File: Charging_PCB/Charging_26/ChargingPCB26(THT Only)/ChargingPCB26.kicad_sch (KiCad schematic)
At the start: 50 parts, among them J1 Molex6pin, K101 Relay_SPDT_Omron_G2RL-1, K102 Relay_SPDT_Omron_G2RL-1, Q1 NMOS, Q103 Q_NPN_BEC, Q104 Q_NPN_BEC, Q105 Q_NPN_BEC, Q106 Q_NPN_BEC, Q2 NMOS, Q3 NMOS, Q4 NMOS, SW101 SW_Omron_B3FS, SW102 SW_Omron_B3FS, U1 SFH617A-1, U107 LM7805_TO220, U2 SFH617A-1, U5 74LS279, U6 74HC00

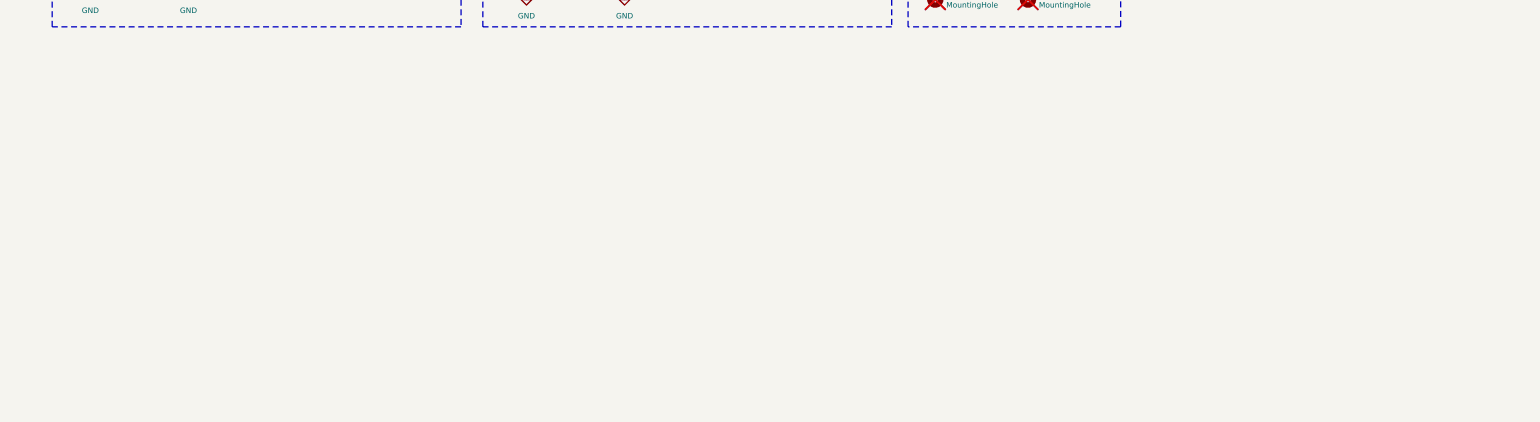
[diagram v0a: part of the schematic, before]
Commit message: changed labeling on charging test schematic
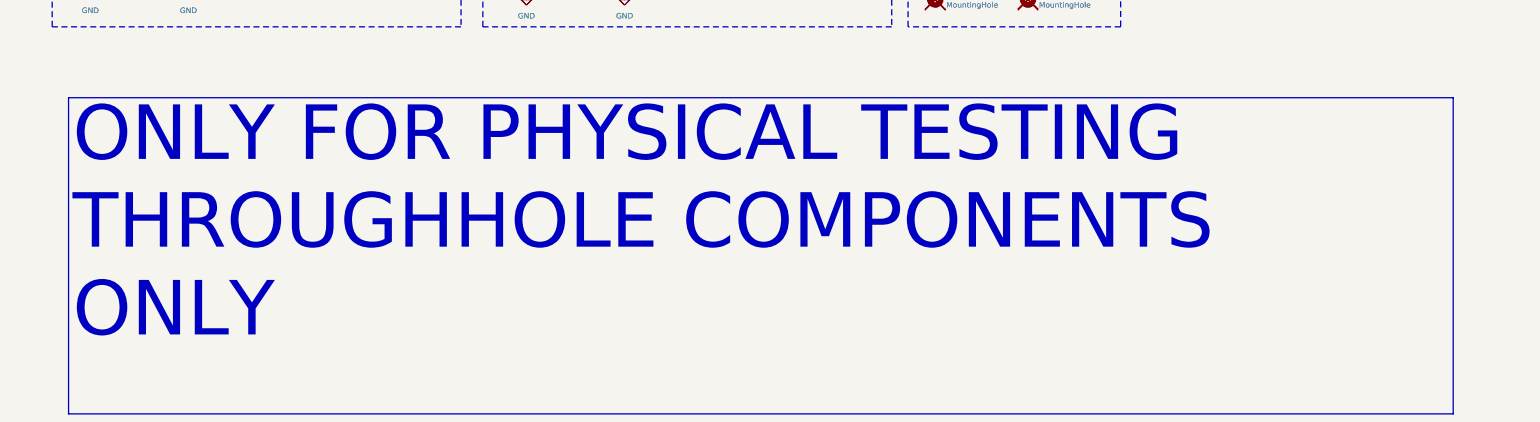
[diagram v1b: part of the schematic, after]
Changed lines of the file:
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@@
+		)
+	)
+	(text_box "ONLY FOR PHYSICAL TESTING THROUGHHOLE COMPONENTS ONLY"
+		(exclude_from_sim no)
+		(at 31.75 311.15 0)
+		(size 322.58 73.66)
+		(margins 0.9525 0.9525 0.9525 0.9525)
+		(stroke
+			(width 0)
+			(type solid)
+		)
+		(fill
+			(type none)
+		)
+		(effects
+			(font
+				(size 12.7 12.7)
+			)
+			(justify left top)
 		)
 	)

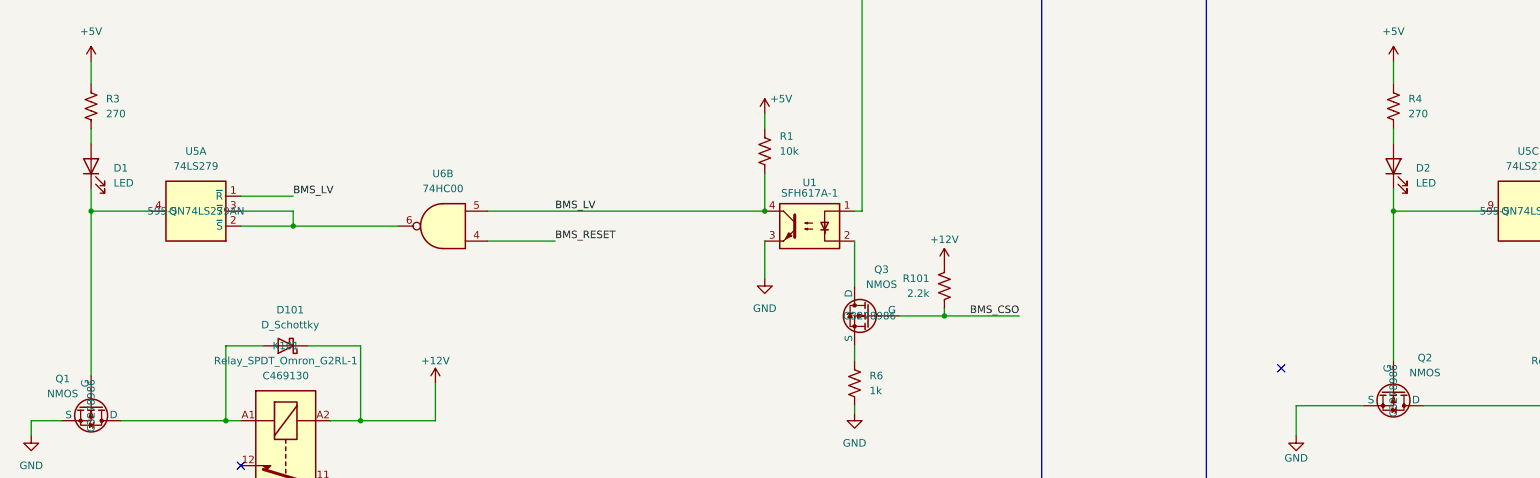
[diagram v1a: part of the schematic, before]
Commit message: changed led resistor values from 270 to 2k
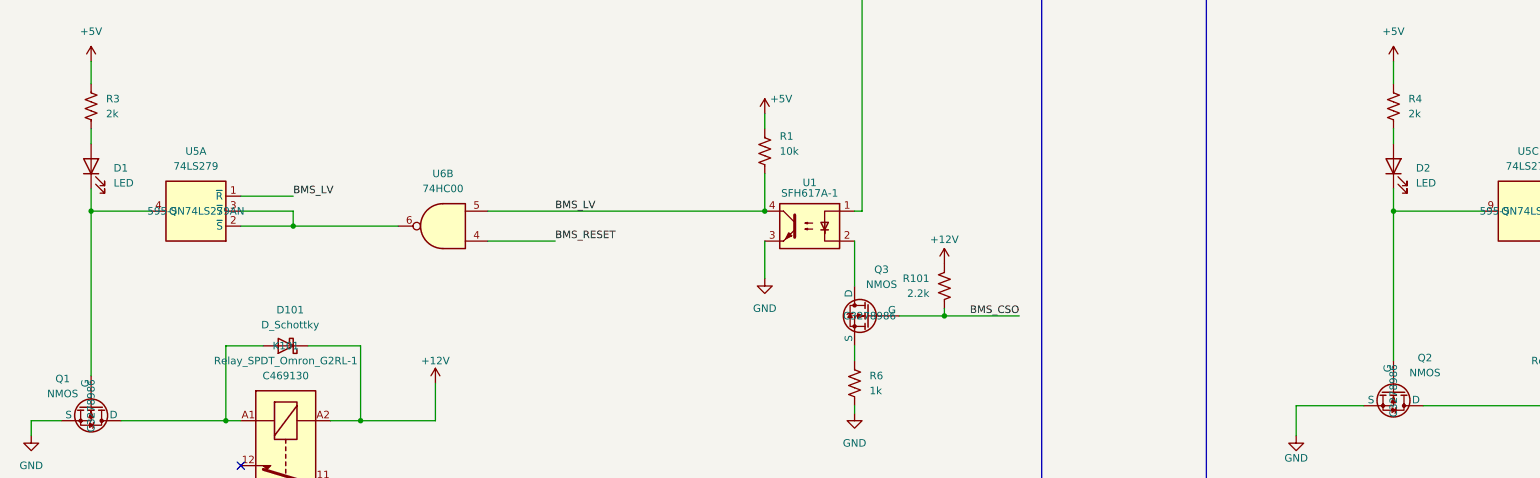
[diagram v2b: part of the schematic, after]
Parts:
- R3, R4: value 270 -> 2k
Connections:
- no-connect marks 16 -> 15
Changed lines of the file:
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@@
 	)
 	(no_connect
-		(at 270.51 123.19)
-	)
-	(no_connect
 		(at 262.89 254)
 	)
@@
 			)
 		)
-		(property "Value" "270"
+		(property "Value" "2k"
 			(at 71.12 80.0099 0)
 			(effects
@@
 			)
 		)
-		(property "Value" "270"
+		(property "Value" "2k"
 			(at 292.1 80.0099 0)
 			(effects

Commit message: fixed logic for bms/imd signals, might still float tell vinh confusing
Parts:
- removed Q3, Q4: NMOS, Package_TO_SOT_THT:TO-251-3_Vertical, symbol Simulation_SPICE:NMOS
- removed R101: 2.2k, Resistor_THT:R_Axial_DIN0207_L6.3mm_D2.5mm_P7.62mm_Horizontal, symbol Device:R_US
- removed R7: 1k, Resistor_THT:R_Axial_DIN0207_L6.3mm_D2.5mm_P7.62mm_Horizontal, symbol Device:R_US
- R5: value 2.2k -> 10k; Digikey 13-MFR-25FTF52-2K2CT-ND -> 1.00KXBK-ND; MPN MFR-25FTF52-2K2 -> MFR-25FBF52-1K
- R6: value 1k -> 10k
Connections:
- net +12V: no longer U1.1
- net BMS_CSO: now also U1.1
- net GND: no longer R5.2
- net IMD_Error: now also R5.2; no longer R5.1
- net at U2.2: now also R5.1
- net at R6.1: now also U1.2
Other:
- note added: "BMS Pulls Low When Ready (High when Fault)"
- note added: "IMD Fault Pulls Low"
- note removed: "https://tinyurl.com/2dm8rjkq"
- moved on the sheet: R6
